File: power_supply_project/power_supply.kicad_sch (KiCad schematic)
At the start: 12 parts, among them J1 Screw_Terminal_01x02, J2 Screw_Terminal_01x02, J4 Conn_01x01_Pin, J5 Conn_01x01_Pin, J6 Conn_01x01_Pin, J7 Conn_01x01_Pin, T1 Transformer_1P_1S, U1 MB10S-13

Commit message: add linear regulator and trimmer resistor to schematic
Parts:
- added J3, J8: Conn_01x01_Pin, Connector_PinHeader_2.54mm:PinHeader_1x01_P2.54mm_Vertical, symbol Connector:Conn_01x01_Pin
- added J9: Conn_01x02_Pin, symbol Connector:Conn_01x02_Pin
- added R2: 2k, Resistor_THT:R_Axial_DIN0207_L6.3mm_D2.5mm_P7.62mm_Horizontal, symbol Device:R
- added R4: 2.2k, Resistor_THT:R_Axial_DIN0207_L6.3mm_D2.5mm_P7.62mm_Horizontal, symbol Device:R
- added R5: CT-6EP103, kody_custom:POT_CT-6EP103_NDC, symbol CT-6EP103:CT-6EP103
- added U2: LM317_TO-220, Package_TO_SOT_THT:TO-220-3_Vertical, symbol Regulator_Linear:LM317_TO-220
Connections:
- net at C1.1, D1.2 (A), J6.1 (Pin_1)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: now also U2.3 (VI); no longer J1.1 (Pin_1)
- net at C1.2, J1.2 (Pin_2), J4.1 (Pin_1)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: now also J3.1 (Pin_1), J9.2 (Pin_2)
- new net: R2.2, R4.1, U2.1 (ADJ)
- new net: J1.1 (Pin_1), J8.1 (Pin_1), R2.1, U2.2 (VO)
- new net: R4.2, R5.3
- new net: J9.1 (Pin_1), R5.2
- no-connect marks 0 -> 1
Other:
- note removed: "test port here"
- moved on the sheet: J1

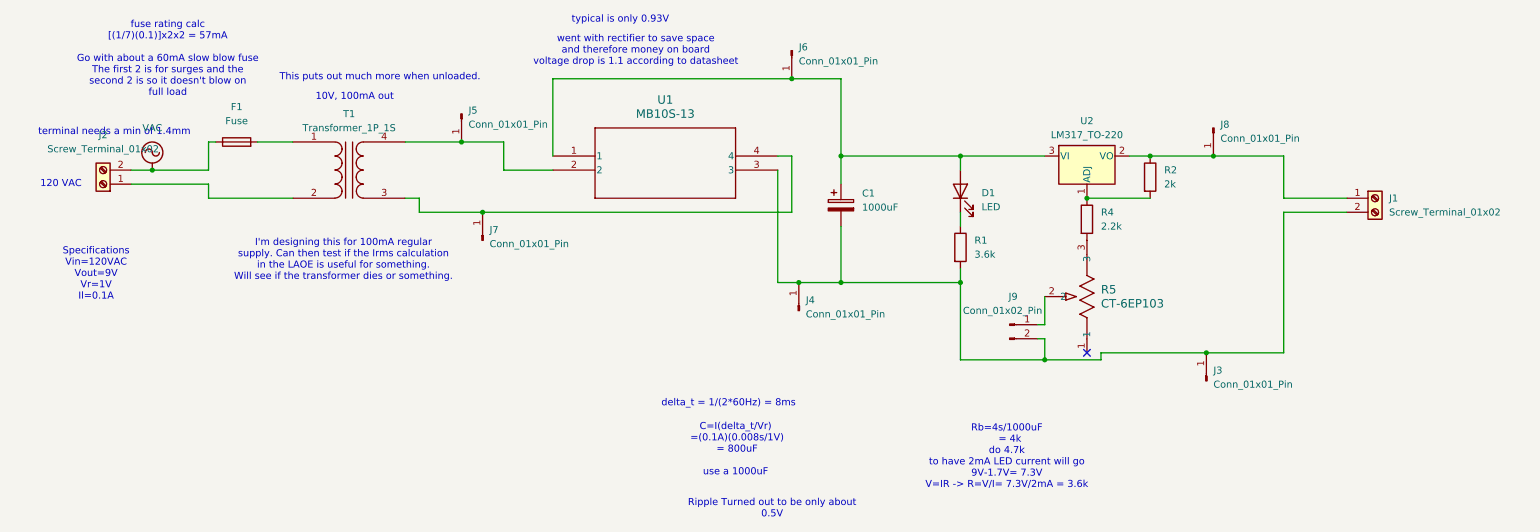
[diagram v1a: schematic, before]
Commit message: fix ERC errors and add footprint for ppk2 test point
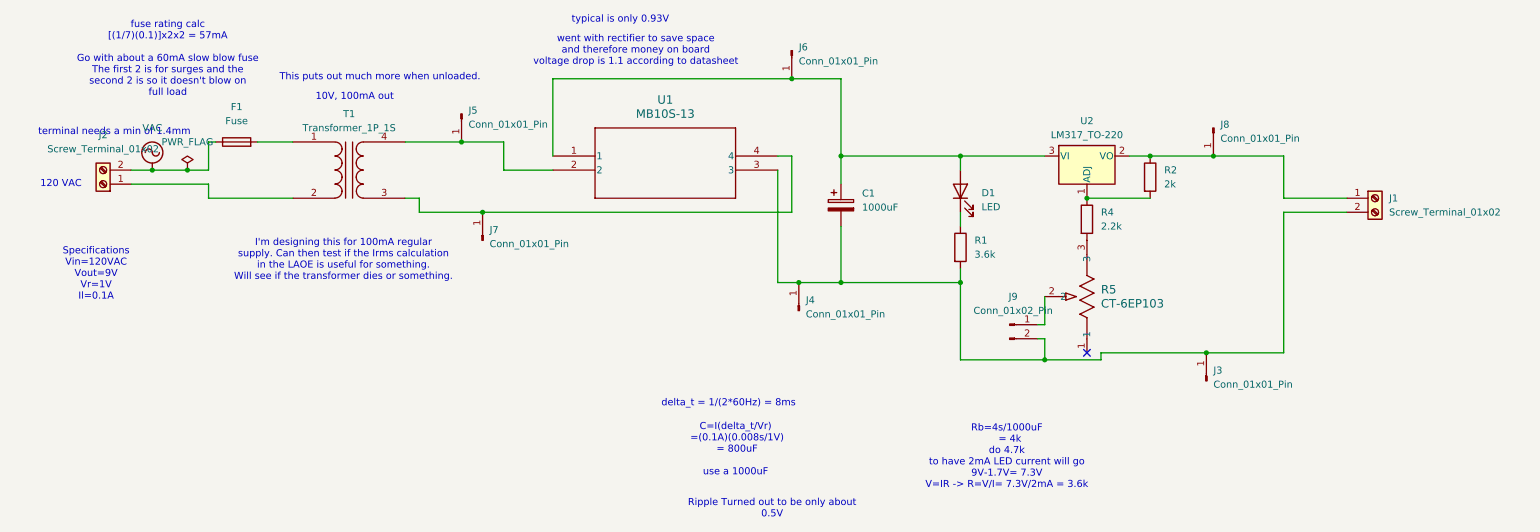
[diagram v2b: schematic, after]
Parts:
- J9: footprint (none) -> Connector_PinHeader_2.54mm:PinHeader_1x02_P2.54mm_Vertical; MFG # (none) -> M20-9990246
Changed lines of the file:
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@@
+	)
+	(junction
+		(at 41.91 60.96)
+		(diameter 0)
+		(color 0 0 0 0)
 	)
 	(junction
@@
 	(wire
 		(pts
+			(xy 181.61 58.42) (xy 196.85 58.42)
+		)
+		(stroke
+			(width 0)
+			(type default)
+		)
+	)
+	(wire
+		(pts
 			(xy 107.95 60.96) (xy 99.06 60.96)
 		)
@@
 	(wire
 		(pts
-			(xy 35.56 60.96) (xy 45.72 60.96)
+			(xy 35.56 60.96) (xy 41.91 60.96)
 		)
 		(stroke
@@
 	(wire
 		(pts
-			(xy 181.61 58.42) (xy 196.85 58.42)
+			(xy 41.91 60.96) (xy 45.72 60.96)
 		)
 		(stroke
@@
 	)
 	(symbol
+		(lib_id "Connector:Conn_01x02_Pin")
+		(at 190.5 88.9 0)
+		(unit 1)
+		(exclude_from_sim no)
+		(in_bom yes)
+		(on_board yes)
+		(dnp no)
+		(fields_autoplaced yes)
+		(property "Reference" "J9"
+			(at 191.135 83.82 0)
+			(effects
+				(font
+					(size 1.27 1.27)
+				)
+			)
+		)
+		(property "Value" "Conn_01x02_Pin"
+			(at 191.135 86.36 0)
+			(effects
+				(font
+					(size 1.27 1.27)
+				)
+			)
+		)
+		(property "Footprint" "Connector_PinHeader_2.54mm:PinHeader_1x02_P2.54mm_Vertical"
+			(at 190.5 88.9 0)
+			(effects
+				(font
+					(size 1.27 1.27)
+				)
+				(hide yes)
+			)
+		)
+		(property "Datasheet" "https://www.digikey.ca/en/products/detail/harwin-inc/M20-9990246/3728226"
+			(at 190.5 88.9 0)
+			(effects
+				(font
+					(size 1.27 1.27)
+				)
+				(hide yes)
+			)
+		)
+		(property "Description" "Generic connector, single row, 01x02, script generated"
+			(at 190.5 88.9 0)
+			(effects
+				(font
+					(size 1.27 1.27)
+				)
+				(hide yes)
+			)
+		)
+		(property "MFG #" "M20-9990246"
+			(at 190.5 88.9 90)
+			(effects
+				(font
+					(size 1.27 1.27)
+				)
+				(hide yes)
+			)
+		)
+		(pin "1"
+		)
+		(pin "2"
+		)
+		(instances
+			(project "power_supply"
+				(path "/0bd9e970-d5a5-422c-a3ec-71316c30eb8e"
+					(reference "J9")
+					(unit 1)
+				)
+			)
+		)
+	)
+	(symbol
 		(lib_id "Device:C_Polarized")
 		(at 160.02 67.31 0)
@@
 	)
 	(symbol
-		(lib_id "Connector:Conn_01x02_Pin")
-		(at 190.5 88.9 0)
-		(unit 1)
-		(exclude_from_sim no)
-		(in_bom yes)
-		(on_board yes)
-		(dnp no)
-		(property "Reference" "J9"
-			(at 191.135 83.82 0)
-			(effects
-				(font
-					(size 1.27 1.27)
-				)
-			)
-		)
-		(property "Value" "Conn_01x02_Pin"
-			(at 189.23 86.36 0)
-			(effects
-				(font
-					(size 1.27 1.27)
-				)
-			)
-		)
-		(property "Footprint" ""
-			(at 190.5 88.9 0)
-			(effects
-				(font
-					(size 1.27 1.27)
-				)
-				(hide yes)
-			)
-		)
-		(property "Datasheet" "~"
-			(at 190.5 88.9 0)
-			(effects
-				(font
-					(size 1.27 1.27)
-				)
-				(hide yes)
-			)
-		)
-		(property "Description" "Generic connector, single row, 01x02, script generated"
-			(at 190.5 88.9 0)
-			(effects
-				(font
-					(size 1.27 1.27)
-				)
-				(hide yes)
-			)
-		)
-		(pin "2"
-		)
-		(pin "1"
-		)
-		(instances
-			(project ""
-				(path "/0bd9e970-d5a5-422c-a3ec-71316c30eb8e"
-					(reference "J9")
-					(unit 1)
-				)
-			)
-		)
-	)
-	(symbol
 		(lib_id "Connector:Screw_Terminal_01x02")
 		(at 26.67 63.5 180)
@@
 		)
 		(property "Footprint" "mb10s_rectifier:TO-269AA_3P8X4P75_DIO-L"
-			(at 107.95 58.42 0)
+			(at 114.554 70.866 0)
 			(effects
 				(font
@@
 		)
 		(property "Datasheet" "https://www.diodes.com/assets/Datasheets/MB10S.pdf"
-			(at 107.95 58.42 0)
+			(at 112.776 67.818 0)
 			(effects
 				(font
@@
 		)
 		(property "Description" "BRIDGE RECT 1PHASE 1KV 800MA MBS"
-			(at 107.95 58.42 0)
+			(at 113.03 73.406 0)
 			(effects
 				(font
@@
 					(unit 1)
 				)
+			)
+		)
+	)
+	(symbol
+		(lib_id "power:PWR_FLAG")
+		(at 41.91 60.96 0)
+		(unit 1)
+		(exclude_from_sim no)
+		(in_bom yes)
+		(on_board yes)
+		(dnp no)
+		(fields_autoplaced yes)
+		(property "Reference" "#FLG02"
+			(at 41.91 59.055 0)
+			(effects
+				(font
+					(size 1.27 1.27)
+				)
+				(hide yes)
+			)
+		)
+		(property "Value" "PWR_FLAG"
+			(at 41.91 55.88 0)
+			(effects
+				(font
+					(size 1.27 1.27)
+				)
+			)
+		)
+		(property "Footprint" ""
+			(at 41.91 60.96 0)
+			(effects
+				(font
+					(size 1.27 1.27)
+				)
+				(hide yes)
+			)
+		)
+		(property "Datasheet" "~"
+			(at 41.91 60.96 0)
+			(effects
+				(font
+					(size 1.27 1.27)
+				)
+				(hide yes)
+			)
+		)
+		(property "Description" "Special symbol for telling ERC where power comes from"
+			(at 41.91 60.96 0)
+			(effects
+				(font
+					(size 1.27 1.27)
+				)
+				(hide yes)
+			)
+		)
+		(pin "1"
+		)
+		(instances
+			(project "power_supply"
+				(path "/0bd9e970-d5a5-422c-a3ec-71316c30eb8e"
+					(reference "#FLG02")
+					(unit 1)
+				)
